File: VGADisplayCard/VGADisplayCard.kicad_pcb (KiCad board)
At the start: 2 copper layers, 58 x 29 mm, 3 parts, among them J2 Bus_PCI_Express_x1

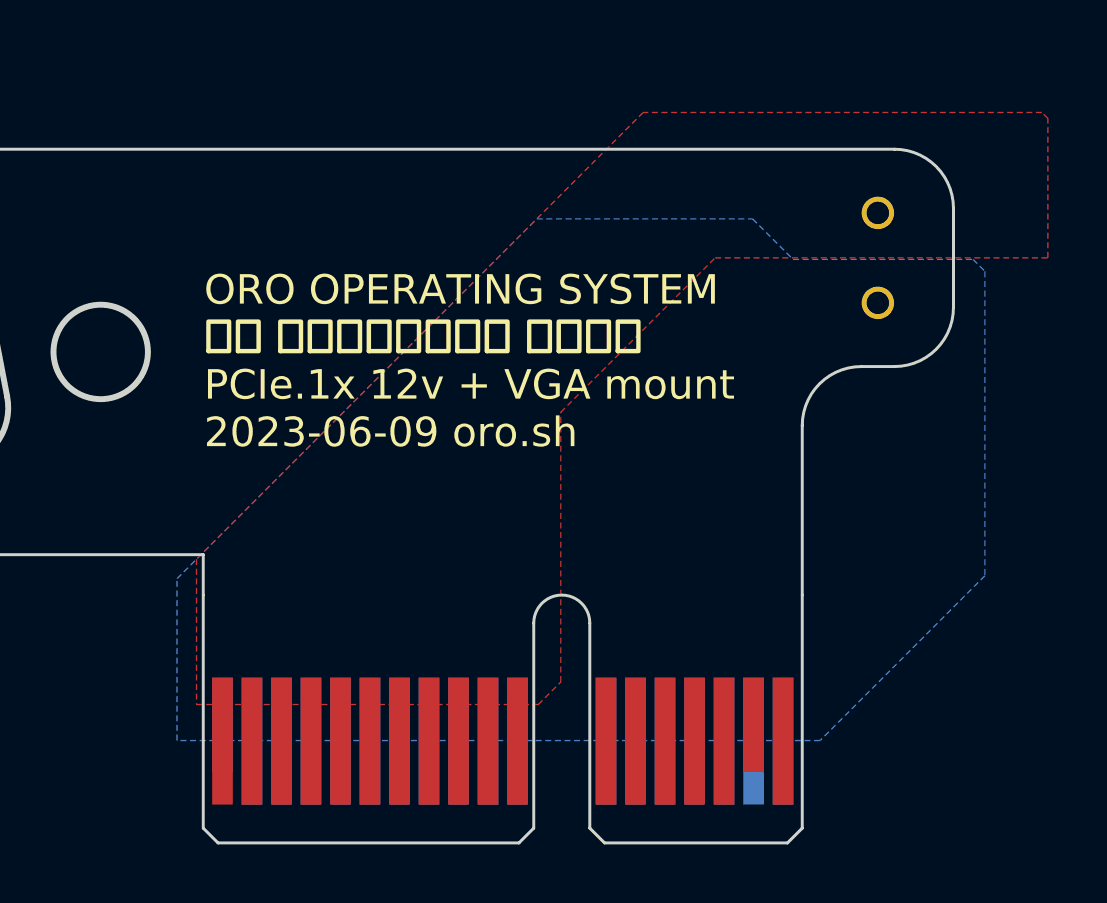
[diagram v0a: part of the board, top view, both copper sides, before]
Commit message: vga mount polish and 2.54mm mount (closes #37)
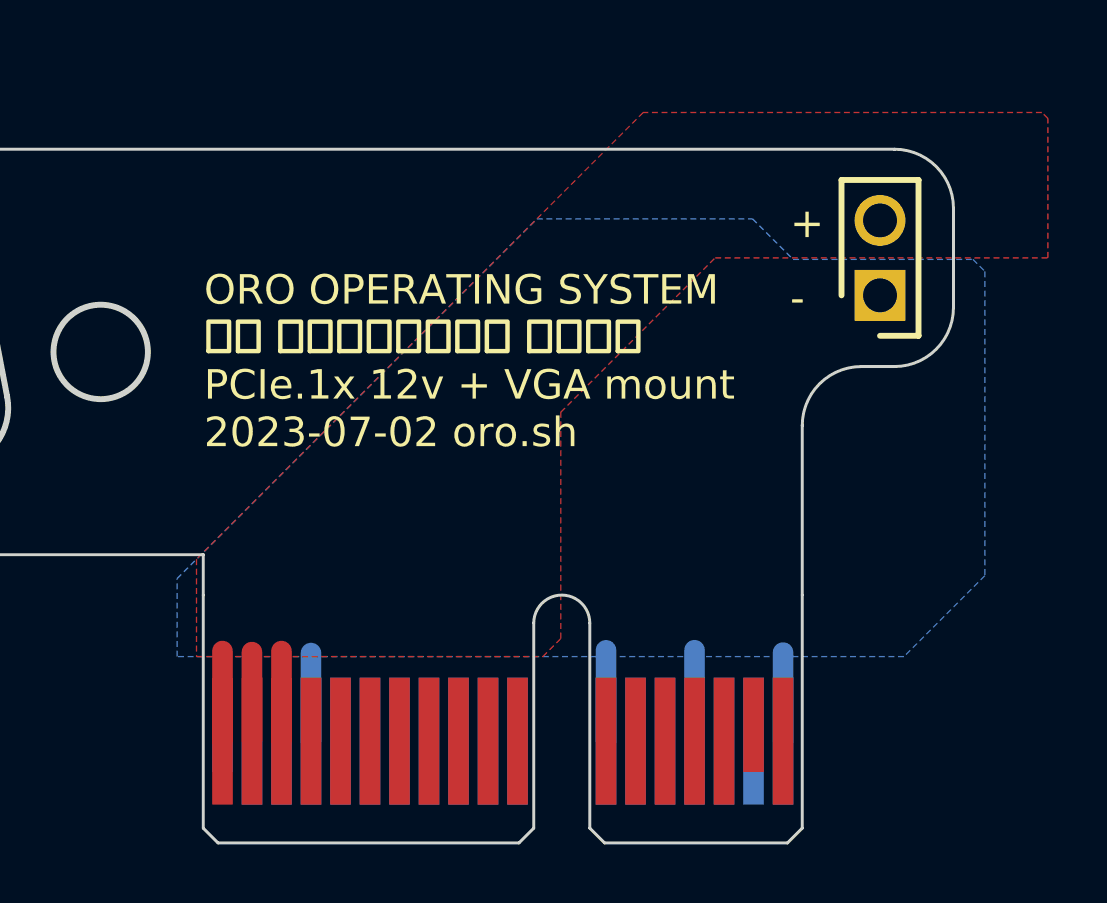
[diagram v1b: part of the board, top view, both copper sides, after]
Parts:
- removed J1, J3: ~, Oro Footprints:DebugPin
- added J4: 2P 2.54, SamacSys_Parts:HDRV2W67P0X254_1X2_508X241X1082P, F.Cu at (173.7, 102.9)
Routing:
- net /GND: track 0.00 -> 12.1 mm
- net /+12V: track 0.00 -> 9.12 mm
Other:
- board text added: "+"
- board text added: "-"
- board text added: "ORO OPERATING SYSTEM オロ オペレーティング システム PCIe.1x 12v + VGA mount 2023-07-02 oro.sh"
- board text removed: "ORO OPERATING SYSTEM オロ オペレーティング システム PCIe.1x 12v + VGA mount 2023-06-09 oro.sh"
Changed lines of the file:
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@@
   (title_block
     (title "PCIe.1x 12v Supply + VGA Mount")
-    (date "2023-06-09")
-    (rev "1")
+    (date "2023-07-02")
+    (rev "2")
     (company "Oro Operating System")
     (comment 1 "://oro.sh")
@@
       (net 22 "/GND") (pinfunction "GND") (pintype "passive"))
   )
-  (footprint "Oro Footprints:DebugPin" (layer "F.Cu")
-    (at 173.6627 100.076)
+  (footprint "SamacSys_Parts:HDRV2W67P0X254_1X2_508X241X1082P" (layer "F.Cu")
+    (at 173.736 102.87 90)
+    (descr "10129378-902003BLF")
+    (tags "Connector")
+    (property "Arrow Part Number" "")
+    (property "Arrow Price/Stock" "")
+    (property "Description" "EconoStik 2.54mm, Board to Board Connector, Unshrouded Verticl Header, Through Hole, Single Row, 2 Positions, 2.54 mm (0.100in) Pitch.")
+    (property "Height" "10.82")
+    (property "Manufacturer_Name" "Amphenol Communication Solutions")
+    (property "Manufacturer_Part_Number" "10129378-902003BLF")
+    (property "Mouser Part Number" "649-1012937890203BLF")
+    (property "Mouser Price/Stock" "https://www.mouser.co.uk/ProductDetail/Amphenol-FCI/10129378-902003BLF?qs=0lQeLiL1qyZU%252BgRaQ8FKPg%3D%3D")
     (property "Sheetfile" "VGADisplayCard.kicad_sch")
     (property "Sheetname" "")
-    (property "Sim.Enable" "0")
-    (property "exclude_from_bom" "")
-    (attr through_hole exclude_from_bom)
-    (fp_text reference "J1" (at 0 -1.27 unlocked) (layer "F.SilkS") hide
-        (effects (font (size 1 1) (thickness 0.15)))
+    (property "ki_description" "EconoStik 2.54mm, Board to Board Connector, Unshrouded Verticl Header, Through Hole, Single Row, 2 Positions, 2.54 mm (0.100in) Pitch.")
+    (attr through_hole)
+    (fp_text reference "J4" (at 0 0 90) (layer "F.SilkS") hide
+        (effects (font (size 1.27 1.27) (thickness 0.254)))
     )
-    (fp_text value "~" (at 0 1 unlocked) (layer "F.Fab") hide
-        (effects (font (size 1 1) (thickness 0.15)))
+    (fp_text value "2P 2.54" (at 0 0 90) (layer "F.SilkS") hide
+        (effects (font (size 1.27 1.27) (thickness 0.254)))
     )
-    (pad "1" thru_hole circle (at 0 0) (size 1.1 1.1) (drill 0.762) (layers "*.Cu" "*.Mask")
-      (net 21 "/+12V") (pintype "passive"))
-  )
-  (footprint "Oro Footprints:DebugPin" (layer "F.Cu")
-    (at 173.6627 103.124)
-    (property "Sheetfile" "VGADisplayCard.kicad_sch")
-    (property "Sheetname" "")
-    (property "Sim.Enable" "0")
-    (property "exclude_from_bom" "")
-    (attr through_hole exclude_from_bom)
-    (fp_text reference "J3" (at 0 -1.27 unlocked) (layer "F.SilkS") hide
-        (effects (font (size 1 1) (thickness 0.15)))
+    (fp_text user "${REFERENCE}" (at 0 0 90) (layer "F.Fab")
+        (effects (font (size 1.27 1.27) (thickness 0.254)))
     )
-    (fp_text value "~" (at 0 1 unlocked) (layer "F.Fab") hide
-        (effects (font (size 1 1) (thickness 0.15)))
+    (fp_line (start -1.37 0) (end -1.37 1.305)
+      (stroke (width 0.2) (type solid)) (layer "F.SilkS"))
+    (fp_line (start -1.37 1.305) (end 3.91 1.305)
+      (stroke (width 0.2) (type solid)) (layer "F.SilkS"))
+    (fp_line (start 3.91 -1.305) (end 0 -1.305)
+      (stroke (width 0.2) (type solid)) (layer "F.SilkS"))
+    (fp_line (start 3.91 1.305) (end 3.91 -1.305)
+      (stroke (width 0.2) (type solid)) (layer "F.SilkS"))
+    (fp_line (start -1.62 -1.555) (end 4.16 -1.555)
+      (stroke (width 0.05) (type solid)) (layer "F.CrtYd"))
+    (fp_line (start -1.62 1.555) (end -1.62 -1.555)
+      (stroke (width 0.05) (type solid)) (layer "F.CrtYd"))
+    (fp_line (start 4.16 -1.555) (end 4.16 1.555)
+      (stroke (width 0.05) (type solid)) (layer "F.CrtYd"))
+    (fp_line (start 4.16 1.555) (end -1.62 1.555)
+      (stroke (width 0.05) (type solid)) (layer "F.CrtYd"))
+    (fp_line (start -1.37 -1.305) (end 3.91 -1.305)
+      (stroke (width 0.1) (type solid)) (layer "F.Fab"))
+    (fp_line (start -1.37 1.305) (end -1.37 -1.305)
+      (stroke (width 0.1) (type solid)) (layer "F.Fab"))
+    (fp_line (start 3.91 -1.305) (end 3.91 1.305)
+      (stroke (width 0.1) (type solid)) (layer "F.Fab"))
+    (fp_line (start 3.91 1.305) (end -1.37 1.305)
+      (stroke (width 0.1) (type solid)) (layer "F.Fab"))
+    (pad "1" thru_hole rect (at 0 0 90) (size 1.725 1.725) (drill 1.15) (layers "*.Cu" "*.Mask")
+      (net 22 "/GND") (pinfunction "1") (pintype "passive"))
+    (pad "2" thru_hole circle (at 2.54 0 90) (size 1.725 1.725) (drill 1.15) (layers "*.Cu" "*.Mask")
+      (net 21 "/+12V") (pinfunction "2") (pintype "passive"))
+    (model "O:\\KiCad Library\\SamacSys_Parts.3dshapes\\10129378-902003BLF.stp"
+      (offset (xyz 0 0 0.2))
+      (scale (xyz 1 1 1))
+      (rotate (xyz 0 90 -90))
     )
-    (pad "1" thru_hole circle (at 0 0) (size 1.1 1.1) (drill 0.762) (layers "*.Cu" "*.Mask")
-      (net 22 "/GND") (pintype "passive"))
   )
   (gr_line (start 128.551687 90.308758) (end 128.547621 90.470034)
@@
   (gr_line (start 118.1862 109.6584) (end 118.1862 86.074)
     (stroke (width 0.1) (type default)) (layer "Edge.Cuts"))
-  (gr_text "ORO OPERATING SYSTEM\nオロ オペレーティング システム\nPCIe.1x 12v + VGA mount\n2023-06-09 oro.sh" (at 150.8252 108.1024) (layer "F.SilkS")
+  (gr_text "+" (at 170.688 101.0175) (layer "F.SilkS")
     (effects (font (size 1 1) (thickness 0.15)) (justify left bottom))
   )
+  (gr_text "ORO OPERATING SYSTEM\nオロ オペレーティング システム\nPCIe.1x 12v + VGA mount\n2023-07-02 oro.sh" (at 150.8252 108.1024) (layer "F.SilkS")
+    (effects (font (size 1 1) (thickness 0.15)) (justify left bottom))
+  )
+  (gr_text "-" (at 170.688 103.5575) (layer "F.SilkS")
+    (effects (font (size 1 1) (thickness 0.15)) (justify left bottom))
+  )
+  (segment (start 151.4502 117.978) (end 151.4502 114.925) (width 0.7) (layer "F.Cu") (net 21))
+  (segment (start 153.4502 117.978) (end 153.4502 114.9262) (width 0.7) (layer "F.Cu") (net 21))
+  (segment (start 152.4502 117.978) (end 152.4502 114.961) (width 0.7) (layer "F.Cu") (net 21))
+  (segment (start 167.4502 117.978) (end 167.4502 114.8962) (width 0.7) (layer "B.Cu") (net 22))
+  (segment (start 154.4502 117.978) (end 154.4502 114.993) (width 0.7) (layer "B.Cu") (net 22))
+  (segment (start 170.4502 117.978) (end 170.4502 114.9766) (width 0.7) (layer "B.Cu") (net 22))
+  (segment (start 164.4502 117.978) (end 164.4502 114.899) (width 0.7) (layer "B.Cu") (net 22))
   (zone (net 21) (net_name "/+12V") (layer "F.Cu") (name "VCC") (hatch edge 0.5)
     (connect_pads (clearance 0.5))
@@
     (polygon
       (pts
-        (xy 150.5712 116.7384)
-        (xy 162.1536 116.7384)
-        (xy 162.9156 115.9764)
+        (xy 150.5712 115.1128)
+        (xy 162.306 115.1128)
+        (xy 162.9156 114.5032)
         (xy 162.9156 106.8324)
         (xy 168.148 101.6)
@@
     (polygon
       (pts
-        (xy 171.704 117.9576)
-        (xy 149.9108 117.9576)
+        (xy 174.5488 115.1128)
+        (xy 149.9108 115.1128)
         (xy 149.9108 112.4712)
         (xy 162.1028 100.2792)
@@
     )
   )
-  (group "" (id 82406ba9-c7a5-4aba-8187-649cd53fb87d)
-    (members
-      e67ad671-66a6-4edf-a851-4e0ada14d3be
-      ecf319d1-0ae4-4fa9-b85a-86155c56a7d2
-    )
-  )
